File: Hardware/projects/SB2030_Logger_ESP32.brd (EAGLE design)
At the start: 36.5 x 80 mm, 34 parts, among them SW1 CKTACTSWITCH, U1 ESP-WROOM-32, U2 MCP2562, U3 NCP1117ST50T3G, U4 NCP1117ST33T3G, U5 SN65C1168PWR, X1 1751280

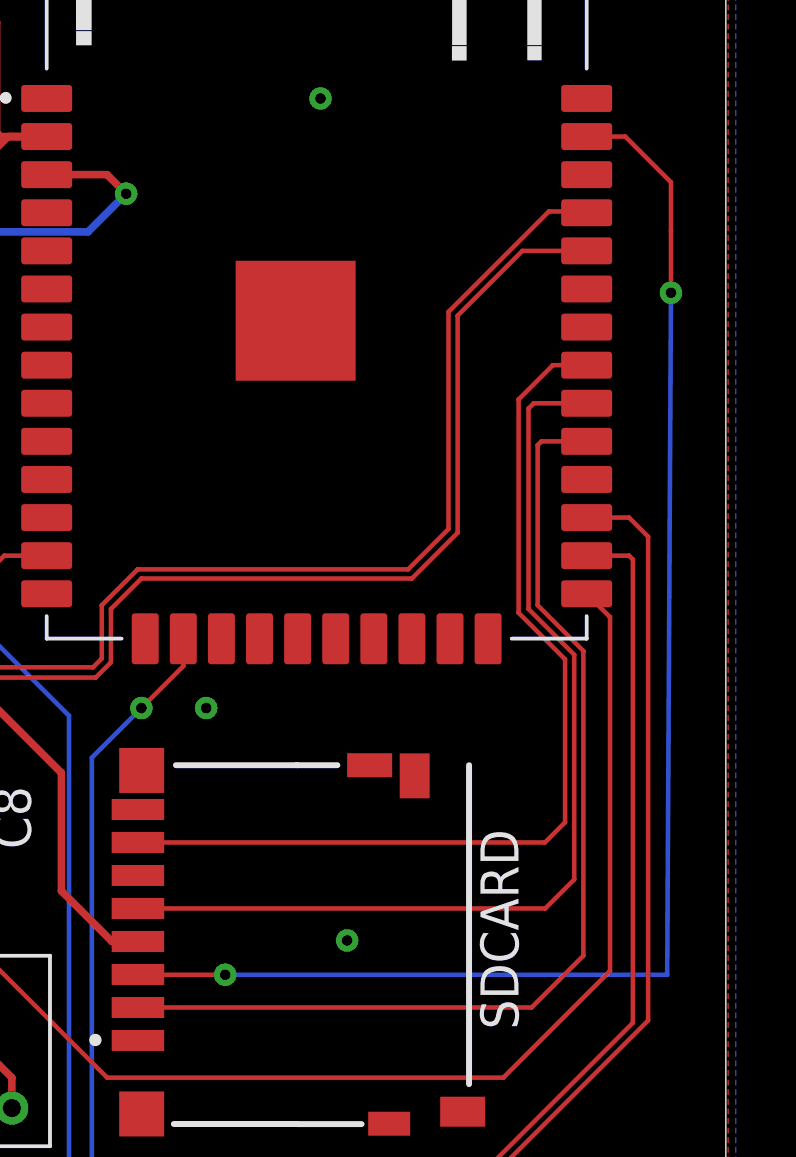
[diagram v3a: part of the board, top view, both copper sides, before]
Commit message: Added updates for reference hardware prototype, and prototype PCB for development boards.
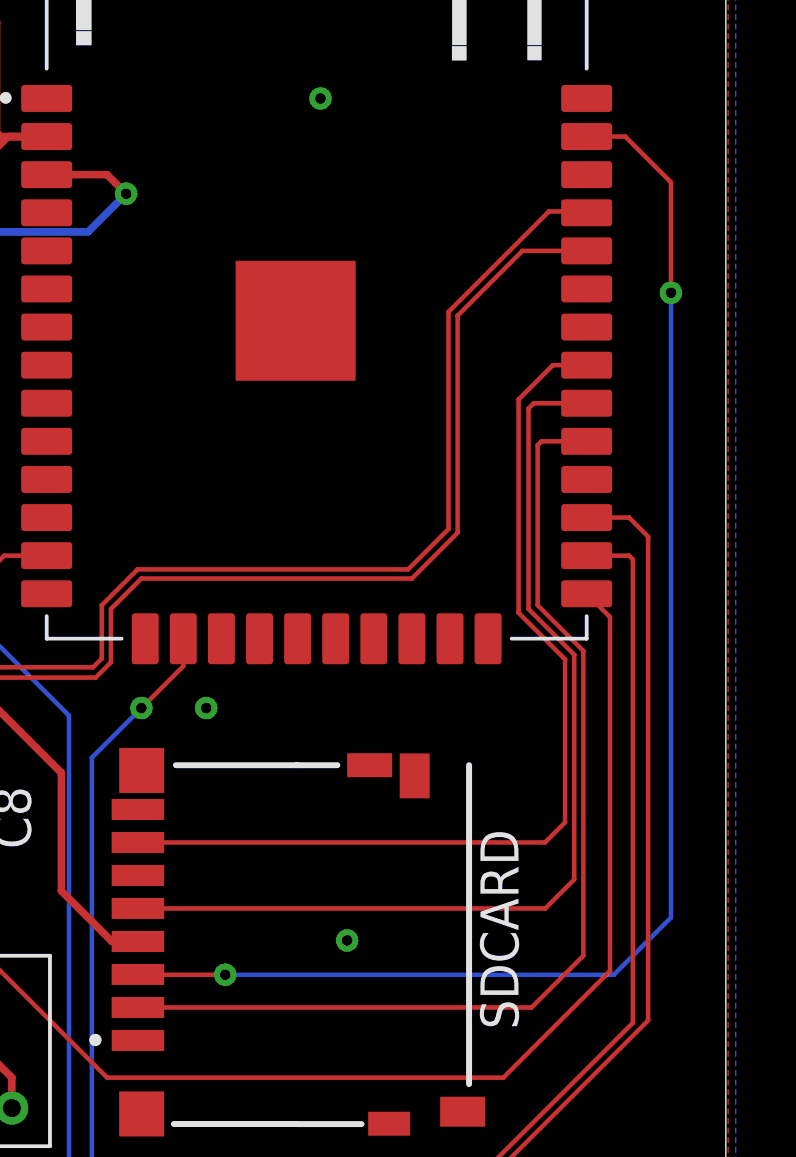
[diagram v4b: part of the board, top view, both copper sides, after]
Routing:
- net N$8: track 47.5 -> 46.7 mm
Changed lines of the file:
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@@
 <drawing>
 <settings>
-<setting alwaysvectorfont="no"/>
+<setting alwaysvectorfont="yes"/>
 <setting verticaltext="up"/>
 </settings>
@@
 <contactref element="SDCARD" pad="3"/>
 <wire x1="33.147" y1="70.485" x2="31.86" y2="70.485" width="0.1524" layer="1"/>
-<wire x1="34.671" y1="67.35618125" x2="34.671" y2="67.31" width="0.1524" layer="1"/>
 <via x="34.671" y="65.278" extent="1-16" drill="0.35"/>
-<wire x1="34.671" y1="67.31" x2="34.671" y2="65.278" width="0.1524" layer="1"/>
-<wire x1="34.671" y1="65.278" x2="34.544" y2="42.545" width="0.1524" layer="16"/>
-<wire x1="34.544" y1="42.545" x2="19.812" y2="42.545" width="0.1524" layer="16"/>
+<wire x1="34.671" y1="68.961" x2="34.671" y2="65.278" width="0.1524" layer="1"/>
+<wire x1="34.671" y1="65.278" x2="34.79729375" y2="65.15170625" width="0.1524" layer="16"/>
 <via x="19.812" y="42.545" extent="1-16" drill="0.35"/>
 <wire x1="19.812" y1="42.545" x2="16.912" y2="42.545" width="0.1524" layer="1"/>
 <wire x1="16.912" y1="42.545" x2="16.902" y2="42.555" width="0.1524" layer="1"/>
-<wire x1="34.671" y1="67.35618125" x2="34.671" y2="68.961" width="0.1524" layer="1"/>
 <wire x1="34.671" y1="68.961" x2="33.147" y2="70.485" width="0.1524" layer="1"/>
+<wire x1="34.671" y1="65.278" x2="34.671" y2="44.45" width="0.1524" layer="16"/>
+<wire x1="34.671" y1="44.45" x2="32.766" y2="42.545" width="0.1524" layer="16"/>
+<wire x1="32.766" y1="42.545" x2="19.812" y2="42.545" width="0.1524" layer="16"/>
 </signal>
 <signal name="N$9">
